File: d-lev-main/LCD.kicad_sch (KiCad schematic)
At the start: 13 parts, among them Q2 MMBT3904

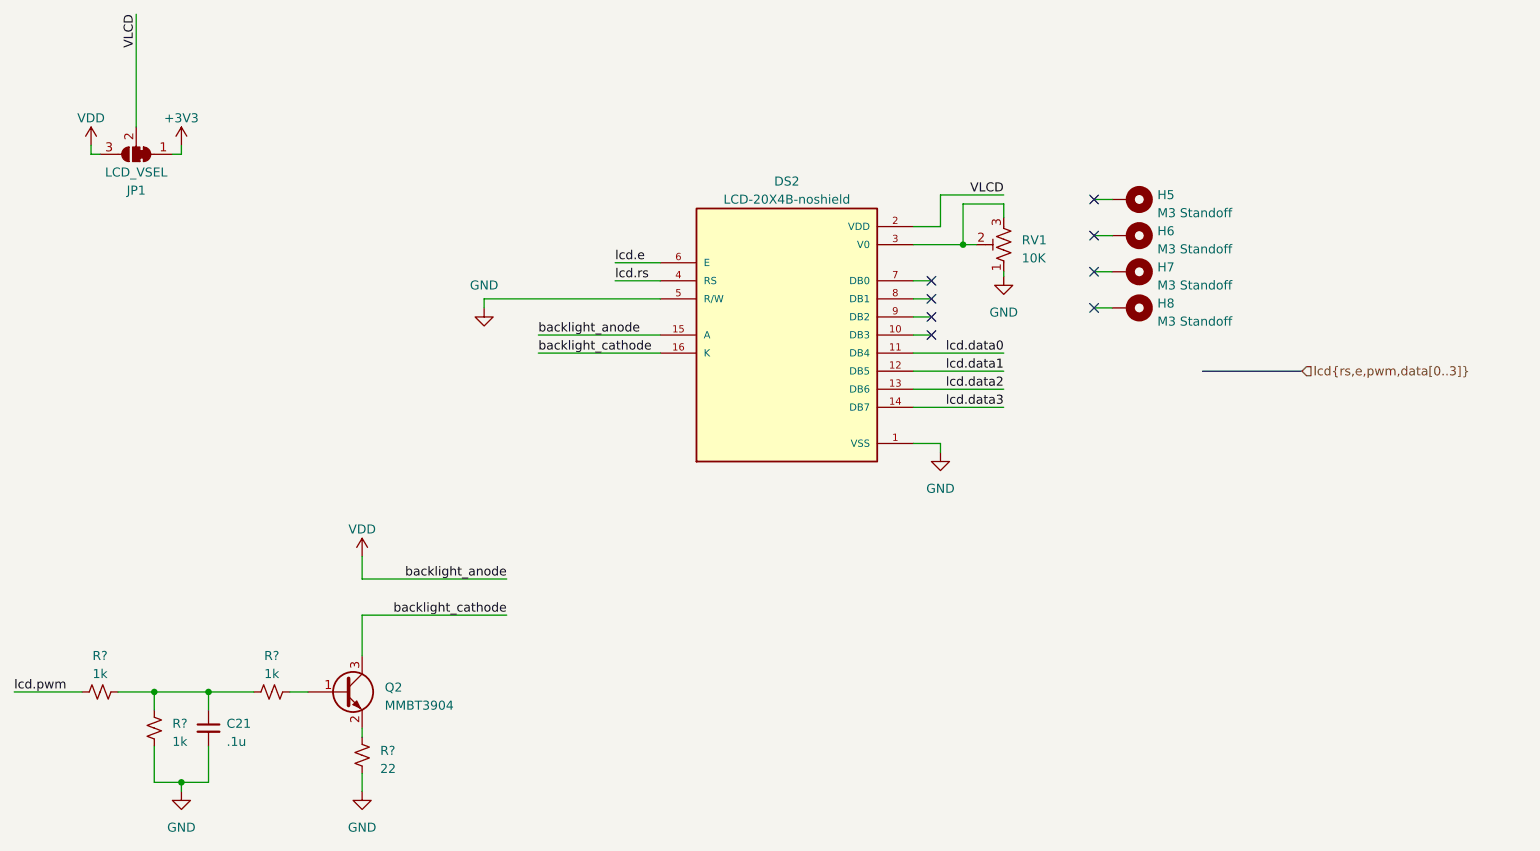
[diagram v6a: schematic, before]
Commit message: round tracks and teardrops
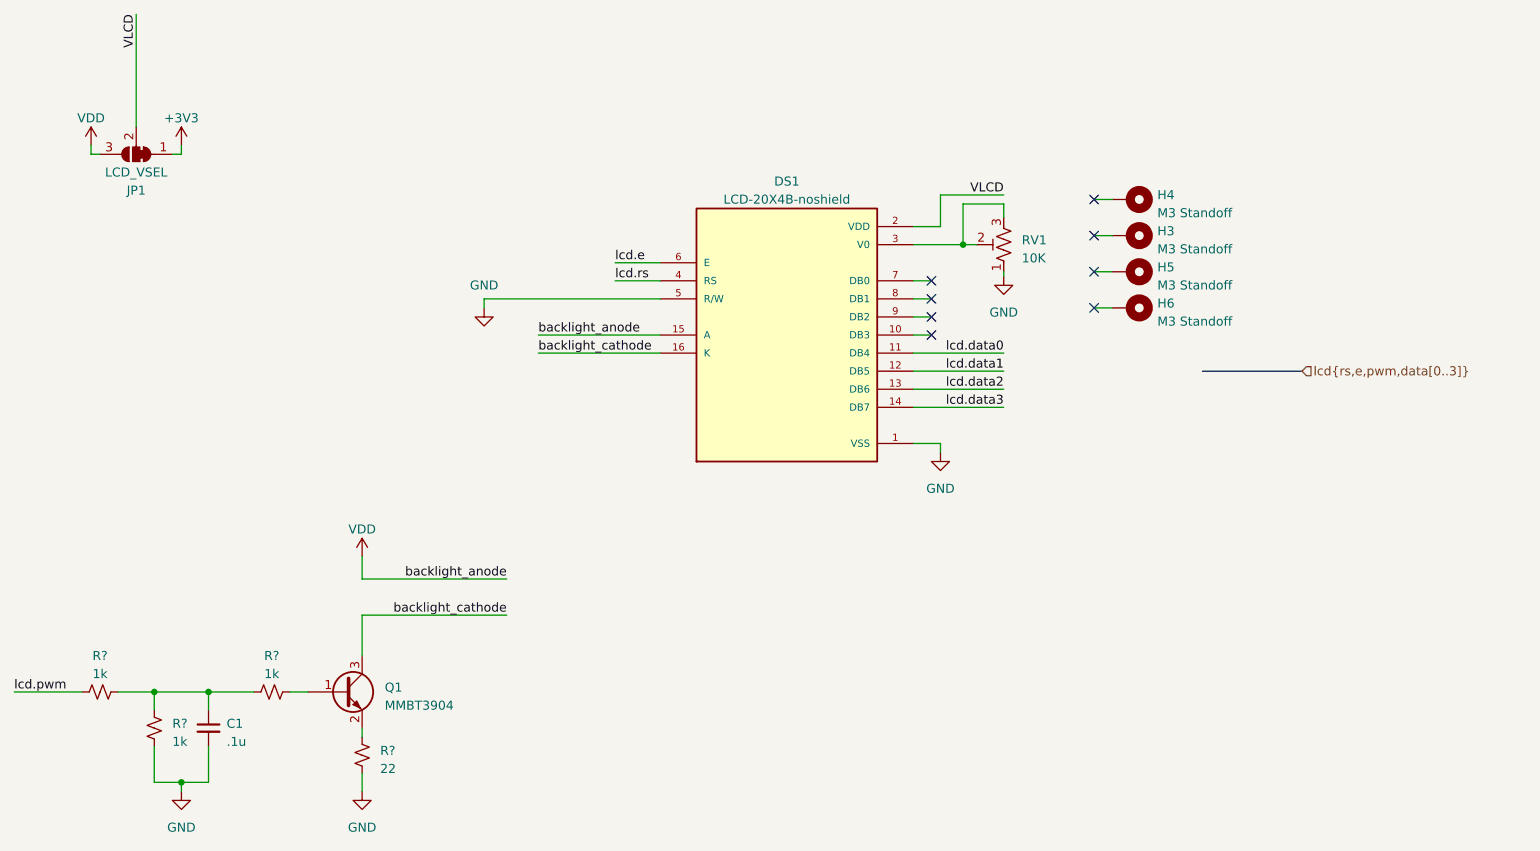
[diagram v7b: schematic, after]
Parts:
- renumbered C21 to C1, DS2 to DS1, H6 to H3, H5 to H4, H7 to H5, H8 to H6, Q2 to Q1
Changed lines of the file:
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@@
   (symbol (lib_id "Mechanical:MountingHole_Pad") (at 198.12 99.06 270) (unit 1)
     (in_bom yes) (on_board yes) (dnp no) (fields_autoplaced)
-    (property "Reference" "H8" (at 201.93 98.425 90)
+    (property "Reference" "H6" (at 201.93 98.425 90)
       (effects (font (size 1.27 1.27)) (justify left))
     )
@@
       (project "dlev-mini"
         (path "/eb5e8bfd-9871-4528-bf57-58851bf63907/2925ec6e-2aba-4938-a246-f8cb5ac94723"
-          (reference "H8") (unit 1)
+          (reference "H6") (unit 1)
         )
       )
@@
         )
         (path "/eb5e8bfd-9871-4528-bf57-58851bf63907/2925ec6e-2aba-4938-a246-f8cb5ac94723"
-          (reference "R8") (unit 1)
+          (reference "R6") (unit 1)
         )
       )
@@
         )
         (path "/eb5e8bfd-9871-4528-bf57-58851bf63907/2925ec6e-2aba-4938-a246-f8cb5ac94723"
-          (reference "R5") (unit 1)
+          (reference "R7") (unit 1)
         )
       )
@@
   (symbol (lib_id "Mechanical:MountingHole_Pad") (at 198.12 93.98 270) (unit 1)
     (in_bom yes) (on_board yes) (dnp no) (fields_autoplaced)
-    (property "Reference" "H7" (at 201.93 93.345 90)
+    (property "Reference" "H5" (at 201.93 93.345 90)
       (effects (font (size 1.27 1.27)) (justify left))
     )
@@
       (project "dlev-mini"
         (path "/eb5e8bfd-9871-4528-bf57-58851bf63907/2925ec6e-2aba-4938-a246-f8cb5ac94723"
-          (reference "H7") (unit 1)
+          (reference "H5") (unit 1)
         )
       )
@@
         )
         (path "/eb5e8bfd-9871-4528-bf57-58851bf63907/2925ec6e-2aba-4938-a246-f8cb5ac94723"
-          (reference "R6") (unit 1)
+          (reference "R5") (unit 1)
         )
       )
@@
   (symbol (lib_id "Transistor_BJT:MMBT3904") (at 87.63 153.035 0) (unit 1)
     (in_bom yes) (on_board yes) (dnp no)
-    (property "Reference" "Q2" (at 93.345 152.4 0)
+    (property "Reference" "Q1" (at 93.345 152.4 0)
       (effects (font (size 1.27 1.27)) (justify left))
     )
@@
       (project "dlev-mini"
         (path "/eb5e8bfd-9871-4528-bf57-58851bf63907/2925ec6e-2aba-4938-a246-f8cb5ac94723"
-          (reference "Q2") (unit 1)
+          (reference "Q1") (unit 1)
         )
       )
@@
   (symbol (lib_id "assorted:LCD-20X4B-noshield") (at 149.86 102.87 0) (unit 1)
     (in_bom yes) (on_board yes) (dnp no) (fields_autoplaced)
-    (property "Reference" "DS2" (at 149.86 81.28 0)
+    (property "Reference" "DS1" (at 149.86 81.28 0)
       (effects (font (size 1.27 1.27)))
     )
@@
       (project "dlev-mini"
         (path "/eb5e8bfd-9871-4528-bf57-58851bf63907/2925ec6e-2aba-4938-a246-f8cb5ac94723"
-          (reference "DS2") (unit 1)
+          (reference "DS1") (unit 1)
         )
       )
@@
   (symbol (lib_id "Device:C_Small") (at 68.58 158.115 0) (unit 1)
     (in_bom yes) (on_board yes) (dnp no) (fields_autoplaced)
-    (property "Reference" "C21" (at 71.12 157.4863 0)
+    (property "Reference" "C1" (at 71.12 157.4863 0)
       (effects (font (size 1.27 1.27)) (justify left))
     )
@@
       (project "dlev-mini"
         (path "/eb5e8bfd-9871-4528-bf57-58851bf63907/2925ec6e-2aba-4938-a246-f8cb5ac94723"
-          (reference "C21") (unit 1)
+          (reference "C1") (unit 1)
         )
       )
@@
   (symbol (lib_id "Mechanical:MountingHole_Pad") (at 198.12 83.82 270) (unit 1)
     (in_bom yes) (on_board yes) (dnp no) (fields_autoplaced)
-    (property "Reference" "H5" (at 201.93 83.185 90)
+    (property "Reference" "H4" (at 201.93 83.185 90)
       (effects (font (size 1.27 1.27)) (justify left))
     )
@@
       (project "dlev-mini"
         (path "/eb5e8bfd-9871-4528-bf57-58851bf63907/2925ec6e-2aba-4938-a246-f8cb5ac94723"
-          (reference "H5") (unit 1)
+          (reference "H4") (unit 1)
         )
       )
@@
   (symbol (lib_id "Mechanical:MountingHole_Pad") (at 198.12 88.9 270) (unit 1)
     (in_bom yes) (on_board yes) (dnp no) (fields_autoplaced)
-    (property "Reference" "H6" (at 201.93 88.265 90)
+    (property "Reference" "H3" (at 201.93 88.265 90)
       (effects (font (size 1.27 1.27)) (justify left))
     )
@@
       (project "dlev-mini"
         (path "/eb5e8bfd-9871-4528-bf57-58851bf63907/2925ec6e-2aba-4938-a246-f8cb5ac94723"
-          (reference "H6") (unit 1)
+          (reference "H3") (unit 1)
         )
       )
@@
         )
         (path "/eb5e8bfd-9871-4528-bf57-58851bf63907/2925ec6e-2aba-4938-a246-f8cb5ac94723"
-          (reference "R7") (unit 1)
-        )
-      )
+          (reference "R4") (unit 1)
+        )
+      )

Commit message: Add iBOMs and additional part numbers
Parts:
- added J6: LCD_CONN, d-lev:ERM2004-2, symbol Connector:Conn_01x16_Socket
- C1: value .1u -> 100n; MPN (none) -> GRM188R71E104KA01D; Notes (none) -> Common; Supplier (none) -> Digi-Key; Supplier URL (none) -> https://www.digikey.com/en/products/detail/murata-electroni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
- DS1: footprint d-lev:ERM2004-2 -> (none); DNP (none) -> Y; MANUFACTURER Gravitech -> (none); MAXIMUM_PACKAGE_HEIGHT 14 mm -> (none); PARTREV N/A -> (none); STANDARD Manufacturer Recommendations -> (none); Supplier (none) -> Aliexpress; Supplier URL (none) -> https://www.aliexpress.us/item/3256804859233272.html
- H3, H4, H5, H6: value M3 Standoff -> SMTSO-M3-4ET; Supplier (none) -> Aliexpress; Supplier URL (none) -> https://www.aliexpress.us/item/3256803593796853.html
- JP1: DNP (none) -> Y
- Q1: Supplier (none) -> Mouser; Supplier URL (none) -> https://www.mouser.com/ProductDetail/Diodes-Incorporated/MM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
- RV1: value 10K -> 10k; Supplier (none) -> Mouser; Supplier URL (none) -> https://www.mouser.com/ProductDetail/Bourns/TC33X-2-103G
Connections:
- net GND: now also J6.1 (Pin_1), J6.5 (Pin_5); no longer DS1.1 (VSS), DS1.5 (R/W)
- net VDD: now also J6.15 (Pin_15); no longer DS1.15 (A)
- net VLCD: now also J6.2 (Pin_2); no longer DS1.2 (VDD)
- net backlight_cathode: now also J6.16 (Pin_16); no longer DS1.16 (K)
- net lcd.data0: now also J6.11 (Pin_11); no longer DS1.11 (DB4)
- net lcd.data1: now also J6.12 (Pin_12); no longer DS1.12 (DB5)
- net lcd.data2: now also J6.13 (Pin_13); no longer DS1.13 (DB6)
- net lcd.data3: now also J6.14 (Pin_14); no longer DS1.14 (DB7)
- net lcd.e: now also J6.6 (Pin_6); no longer DS1.6 (E)
- net lcd.rs: now also J6.4 (Pin_4); no longer DS1.4 (RS)
- net at RV1.2, RV1.3: now also J6.3 (Pin_3); no longer DS1.3 (V0)
- no-connect marks 8 -> 24
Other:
- note added: "Sloppy, but this is just for the BOM"
- note added: "https://www.aliexpress.us/item/3256805008610566.html"
- moved on the sheet: RV1
